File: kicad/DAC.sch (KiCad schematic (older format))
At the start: 27 parts, among them Q1 Q_DUAL_NMOS_S1G1D2S2G2D1, U3 VRH4801NTX, U7 DS3911, U8 TSV994IPT

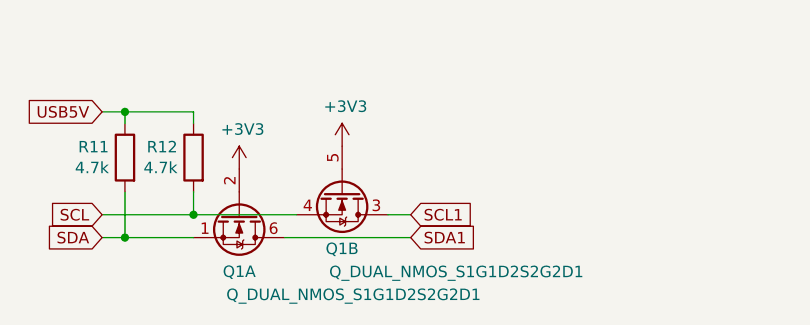
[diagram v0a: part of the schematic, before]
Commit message: replace dual mosfet
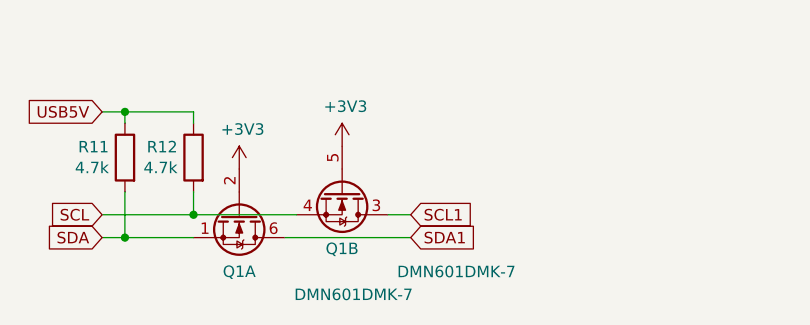
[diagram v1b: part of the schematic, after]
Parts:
- Q1: value Q_DUAL_NMOS_S1G1D2S2G2D1 -> DMN601DMK-7; JLC (none) -> SOT-23-6; LCSC (none) -> C150709
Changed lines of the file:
@@
 AR Path="/63922B28/63AF8507" Ref="Q1"  Part="1"
 F 0 "Q1" V 4849 5600 50  0000 C CNN
-F 1 "Q_DUAL_NMOS_S1G1D2S2G2D1" V 4950 6100 50  0000 C CNN
+F 1 "DMN601DMK-7" V 4950 6100 50  0000 C CNN
 F 2 "Package_TO_SOT_SMD:SOT-23-6_Handsoldering" H 4800 5600 50  0001 C CNN
 F 3 "~" H 4800 5600 50  0001 C CNN
+F 4 "SOT-23-6" H 4600 5600 50  0001 C CNN "JLC"
+F 5 " C150709 " H 4600 5600 50  0001 C CNN "LCSC"
 	1    4600 5600
 	0    1    1    0
@@
 AR Path="/63922B28/63AF850D" Ref="Q1"  Part="2"
 F 0 "Q1" V 5299 5500 50  0000 C CNN
-F 1 "Q_DUAL_NMOS_S1G1D2S2G2D1" V 5400 6000 50  0000 C CNN
+F 1 "DMN601DMK-7" V 5400 6000 50  0000 C CNN
 F 2 "Package_TO_SOT_SMD:SOT-23-6_Handsoldering" H 5250 5500 50  0001 C CNN
 F 3 "~" H 5250 5500 50  0001 C CNN
+F 4 "SOT-23-6" H 5050 5500 50  0001 C CNN "JLC"
+F 5 " C150709 " H 5050 5500 50  0001 C CNN "LCSC"
 	2    5050 5500
 	0    1    1    0

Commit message: usb-c connector update
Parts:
- Q1: ordered (none) -> y
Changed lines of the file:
@@
 F 4 "SOT-23-6" H 4600 5600 50  0001 C CNN "JLC"
 F 5 " C150709 " H 4600 5600 50  0001 C CNN "LCSC"
+F 6 "y" H 4600 5600 50  0001 C CNN "ordered"
 	1    4600 5600
 	0    1    1    0
@@
 F 4 "SOT-23-6" H 5050 5500 50  0001 C CNN "JLC"
 F 5 " C150709 " H 5050 5500 50  0001 C CNN "LCSC"
+F 6 "y" H 5050 5500 50  0001 C CNN "ordered"
 	2    5050 5500
 	0    1    1    0

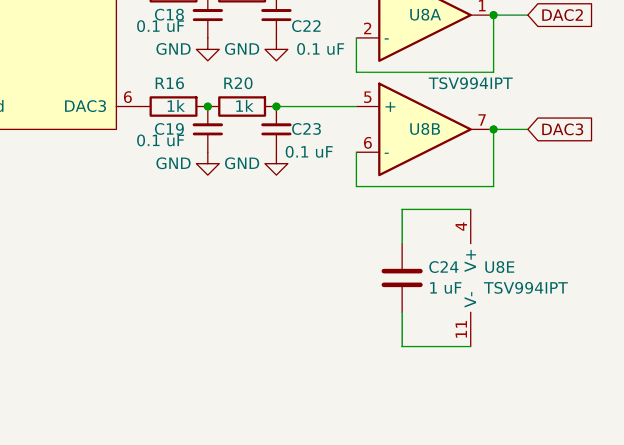
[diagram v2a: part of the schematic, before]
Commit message: connect opamp supply to 4v8 and gnd
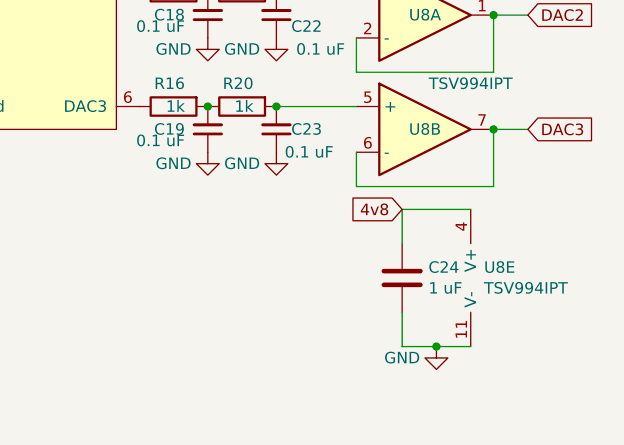
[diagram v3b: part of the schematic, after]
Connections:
- net 4v8: now also C24.1, U8.4 (V+)
- net GND: now also C24.2, U8.11 (V-)
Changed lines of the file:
@@
 	9350 5500 9350 5650
 Wire Wire Line
-	9350 5650 9650 5650
+	9350 5650 9500 5650
 Wire Wire Line
 	8800 3150 9150 3150
@@
 Wire Wire Line
 	4100 3650 4100 3500
+Text GLabel 9350 5050 0    50   Input ~ 0
+4v8
+$Comp
+L power:GND #PWR?
+U 1 1 6437C562
+P 9500 5650
+AR Path="/6437C562" Ref="#PWR?"  Part="1"
+AR Path="/63922B28/6437C562" Ref="#PWR?"  Part="1"
+F 0 "#PWR?" H 9500 5400 50  0001 C CNN
+F 1 "GND" H 9350 5600 50  0000 C CNN
+F 2 "" H 9500 5650 50  0001 C CNN
+F 3 "" H 9500 5650 50  0001 C CNN
+	1    9500 5650
+	1    0    0    -1
+$EndComp
+Connection ~ 9500 5650
+Wire Wire Line
+	9500 5650 9650 5650
 $EndSCHEMATC
